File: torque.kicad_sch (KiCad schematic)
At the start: 30 parts, among them U24 ${SIM.PARAMS}, U25 ${SIM.PARAMS}, U26 ${SIM.PARAMS}, U27 ${SIM.PARAMS}, U28 AD5160, U29 AD5160, U30 AD5160, U31 AD5160, U32 AD5160, U33 AD5160, U34 AD5160, U35 AD5160, U92 ${SIM.PARAMS}

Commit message: Before 10K resistors change
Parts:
- R35, R36, R37, R38, R39, R40, R41, R42, R43: footprint (none) -> Resistor_SMD:R_1206_3216Metric_Pad1.30x1.75mm_HandSolder
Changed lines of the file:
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@@
 			)
 		)
-		(property "Footprint" ""
+		(property "Footprint" "Resistor_SMD:R_1206_3216Metric_Pad1.30x1.75mm_HandSolder"
 			(at 215.9 198.628 90)
 			(effects
@@
 			)
 		)
-		(property "Footprint" ""
+		(property "Footprint" "Resistor_SMD:R_1206_3216Metric_Pad1.30x1.75mm_HandSolder"
 			(at 110.49 195.072 90)
 			(effects
@@
 			)
 		)
-		(property "Footprint" ""
+		(property "Footprint" "Resistor_SMD:R_1206_3216Metric_Pad1.30x1.75mm_HandSolder"
 			(at 110.49 151.892 90)
 			(effects
@@
 			)
 		)
-		(property "Footprint" ""
+		(property "Footprint" "Resistor_SMD:R_1206_3216Metric_Pad1.30x1.75mm_HandSolder"
 			(at 95.25 259.842 90)
 			(effects
@@
 			)
 		)
-		(property "Footprint" ""
+		(property "Footprint" "Resistor_SMD:R_1206_3216Metric_Pad1.30x1.75mm_HandSolder"
 			(at 95.25 214.122 90)
 			(effects
@@
 			)
 		)
-		(property "Footprint" ""
+		(property "Footprint" "Resistor_SMD:R_1206_3216Metric_Pad1.30x1.75mm_HandSolder"
 			(at 110.49 108.712 90)
 			(effects
@@
 			)
 		)
-		(property "Footprint" ""
+		(property "Footprint" "Resistor_SMD:R_1206_3216Metric_Pad1.30x1.75mm_HandSolder"
 			(at 110.49 240.792 90)
 			(effects
@@
 			)
 		)
-		(property "Footprint" ""
+		(property "Footprint" "Resistor_SMD:R_1206_3216Metric_Pad1.30x1.75mm_HandSolder"
 			(at 95.25 170.942 90)
 			(effects
@@
 			)
 		)
-		(property "Footprint" ""
+		(property "Footprint" "Resistor_SMD:R_1206_3216Metric_Pad1.30x1.75mm_HandSolder"
 			(at 95.25 127.762 90)
 			(effects

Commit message: Before capcitor update
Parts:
- R35, R36, R37, R38, R39, R40, R41, R42, R43: value R -> 10k
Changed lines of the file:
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@@
 			)
 		)
-		(property "Value" "R"
+		(property "Value" "10k"
 			(at 213.614 200.152 90)
 			(effects
@@
 			)
 		)
-		(property "Value" "R"
+		(property "Value" "10k"
 			(at 110.49 193.04 90)
 			(effects
@@
 			)
 		)
-		(property "Value" "R"
+		(property "Value" "10k"
 			(at 110.49 149.86 90)
 			(effects
@@
 			)
 		)
-		(property "Value" "R"
+		(property "Value" "10k"
 			(at 95.25 257.81 90)
 			(effects
@@
 			)
 		)
-		(property "Value" "R"
+		(property "Value" "10k"
 			(at 95.25 212.09 90)
 			(effects
@@
 			)
 		)
-		(property "Value" "R"
+		(property "Value" "10k"
 			(at 110.49 106.68 90)
 			(effects
@@
 			)
 		)
-		(property "Value" "R"
+		(property "Value" "10k"
 			(at 110.49 238.76 90)
 			(effects
@@
 			)
 		)
-		(property "Value" "R"
+		(property "Value" "10k"
 			(at 95.25 168.91 90)
 			(effects
@@
 			)
 		)
-		(property "Value" "R"
+		(property "Value" "10k"
 			(at 95.25 125.73 90)
 			(effects

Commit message: updated capacitor values
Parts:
- C61, C62, C63, C64, C65, C66, C67, C68: value C -> 100nF
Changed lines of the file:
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@@
 			)
 		)
-		(property "Value" "C"
+		(property "Value" "100nF"
 			(at 190.5 78.7399 0)
 			(effects
@@
 			)
 		)
-		(property "Value" "C"
+		(property "Value" "100nF"
 			(at 162.56 222.2501 0)
 			(effects
@@
 			)
 		)
-		(property "Value" "C"
+		(property "Value" "100nF"
 			(at 162.56 95.2501 0)
 			(effects
@@
 			)
 		)
-		(property "Value" "C"
+		(property "Value" "100nF"
 			(at 190.5 205.7399 0)
 			(effects
@@
 			)
 		)
-		(property "Value" "C"
+		(property "Value" "100nF"
 			(at 190.5 267.9699 0)
 			(effects
@@
 			)
 		)
-		(property "Value" "C"
+		(property "Value" "100nF"
 			(at 190.5 140.9699 0)
 			(effects
@@
 			)
 		)
-		(property "Value" "C"
+		(property "Value" "100nF"
 			(at 162.56 284.4801 0)
 			(effects
@@
 			)
 		)
-		(property "Value" "C"
+		(property "Value" "100nF"
 			(at 162.56 157.4801 0)
 			(effects

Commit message: Updated: power
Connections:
- net -VCC is gone; now on net GND: U24.4 (V-), U25.4 (V-), U26.4 (V-), U27.4 (V-), U92.4 (V-)
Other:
- moved on the sheet: C61, C62, C63, C64, C65, C66, C67, C68

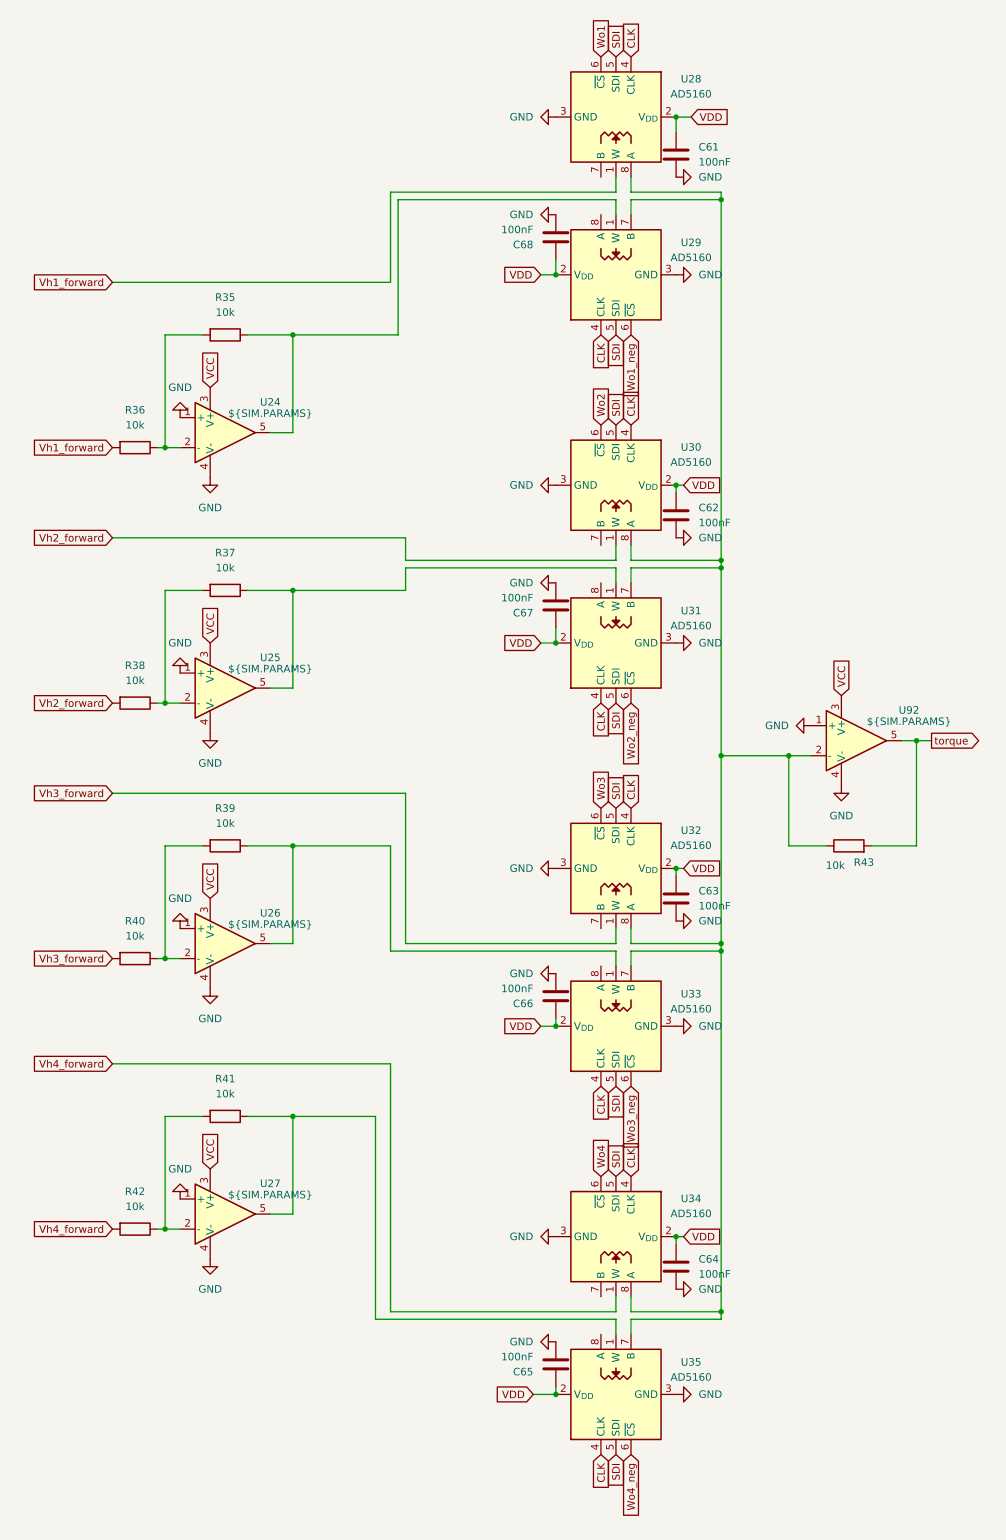
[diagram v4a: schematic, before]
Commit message: Updated: op amps
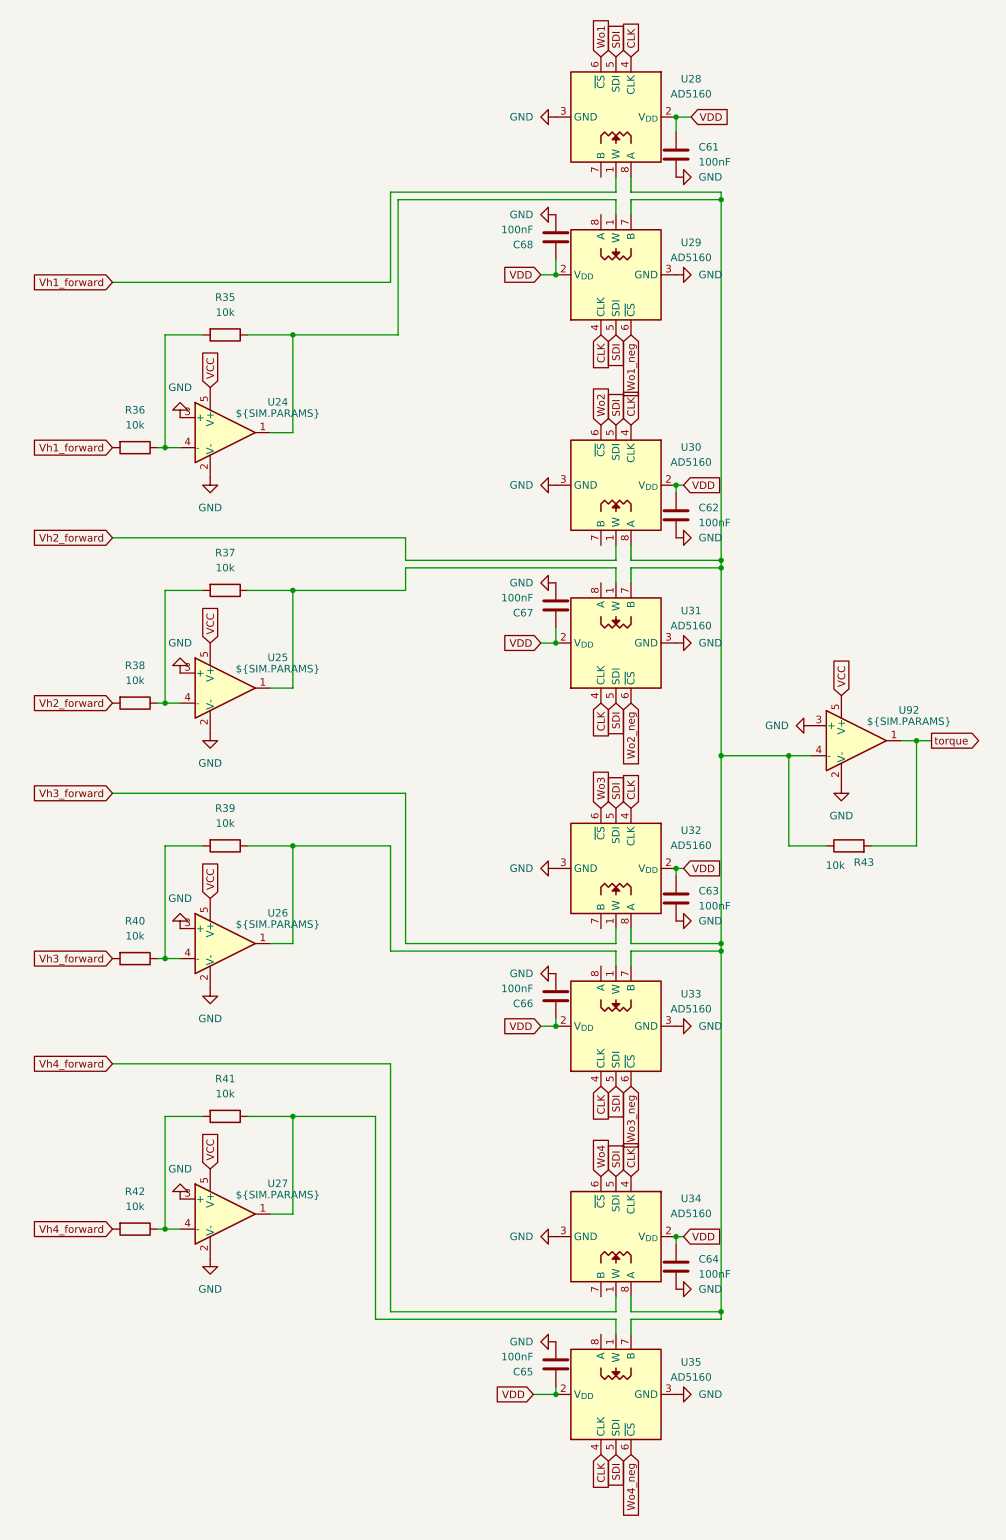
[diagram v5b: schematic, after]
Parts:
- C61, C62, C63, C64, C65, C66, C67, C68: footprint (none) -> Capacitor_SMD:C_1206_3216Metric_Pad1.33x1.80mm_HandSolder
- U24, U25, U26, U27, U92: footprint (none) -> Package_TO_SOT_SMD:SOT-23-5; symbol Simulation_SPICE:OPAMP -> Amplifier_Operational:TLV9061xDBV
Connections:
- net GND: now also U24.2 (V-), U24.3 (+), U25.2 (V-), U25.3 (+), U26.2 (V-), U26.3 (+), U27.2 (V-), U27.3 (+), U92.2 (V-), U92.3 (+); no longer U24.1 (+), U24.4 (V-), U25.1 (+), U25.4 (V-), U26.1 (+), U26.4 (V-), U27.1 (+), U27.4 (V-), U92.1 (+), U92.4 (V-)
- net VCC: now also U24.5 (V+), U25.5 (V+), U26.5 (V+), U27.5 (V+), U92.5 (V+); no longer U24.3 (V+), U25.3 (V+), U26.3 (V+), U27.3 (V+), U92.3 (V+)
- net torque: now also U92.1; no longer U92.5
- net at R43.1, U28.8 (A), U29.7 (B)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: now also U92.4 (-); no longer U92.2 (-)
- net at R37.1, U31.1 (W): now also U25.1; no longer U25.5
- net at R39.1, U33.1 (W): now also U26.1; no longer U26.5
- net at R39.2, R40.1: now also U26.4 (-); no longer U26.2 (-)
- net at R37.2, R38.1: now also U25.4 (-); no longer U25.2 (-)
- net at R41.2, R42.1: now also U27.4 (-); no longer U27.2 (-)
- net at R41.1, U35.1 (W): now also U27.1; no longer U27.5
- net at R35.1, U29.1 (W): now also U24.1; no longer U24.5
- net at R35.2, R36.1: now also U24.4 (-); no longer U24.2 (-)
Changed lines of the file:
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@@
 			)
 		)
-		(property "Footprint" ""
+		(property "Footprint" "Capacitor_SMD:C_1206_3216Metric_Pad1.33x1.80mm_HandSolder"
 			(at 187.6552 83.82 0)
 			(effects
@@
 			)
 		)
-		(property "Footprint" ""
+		(property "Footprint" "Capacitor_SMD:C_1206_3216Metric_Pad1.33x1.80mm_HandSolder"
 			(at 165.4048 218.44 0)
 			(effects
@@
 	)
 	(symbol
-		(lib_id "Simulation_SPICE:OPAMP")
+		(lib_id "Amplifier_Operational:TLV9061xDBV")
 		(at 110.49 170.18 0)
 		(unit 1)
@@
 		(fields_autoplaced yes)
 		(property "Reference" "U25"
-			(at 118.11 165.0298 0)
+			(at 119.38 165.0298 0)
 			(effects
 				(font
@@
 		)
 		(property "Value" "${SIM.PARAMS}"
-			(at 118.11 166.9349 0)
+			(at 119.38 166.9349 0)
 			(effects
 				(font
@@
 			)
 		)
-		(property "Footprint" ""
-			(at 110.49 170.18 0)
+		(property "Footprint" "Package_TO_SOT_SMD:SOT-23-5"
+			(at 95.25 189.23 0)
 			(effects
 				(font
 					(size 1.27 1.27)
 				)
+				(justify left)
 				(hide yes)
 			)
 		)
-		(property "Datasheet" "https://ngspice.sourceforge.io/docs/ngspice-html-manual/manual.xhtml#sec__SUBCKT_Subcircuits"
-			(at 110.49 170.18 0)
+		(property "Datasheet" "https://www.ti.com/lit/ds/symlink/tlv9061.pdf"
+			(at 110.49 149.86 0)
 			(effects
 				(font
@@
 			)
 		)
-		(property "Description" "Operational amplifier, single"
+		(property "Description" "10-MHz, RRIO, CMOS Operational Amplifiers for Cost-Sensitive Systems, SOT-23-5"
 			(at 110.49 170.18 0)
 			(effects
@@
 			)
 		)
-		(property "Footprint" ""
+		(property "Footprint" "Capacitor_SMD:C_1206_3216Metric_Pad1.33x1.80mm_HandSolder"
 			(at 165.4048 90.17 0)
 			(effects
@@
 			)
 		)
-		(property "Footprint" ""
+		(property "Footprint" "Capacitor_SMD:C_1206_3216Metric_Pad1.33x1.80mm_HandSolder"
 			(at 187.6552 209.55 0)
 			(effects
@@
 	)
 	(symbol
-		(lib_id "Simulation_SPICE:OPAMP")
+		(lib_id "Amplifier_Operational:TLV9061xDBV")
 		(at 217.17 179.07 0)
 		(unit 1)
@@
 			)
 		)
-		(property "Footprint" ""
-			(at 217.17 179.07 0)
+		(property "Footprint" "Package_TO_SOT_SMD:SOT-23-5"
+			(at 201.93 198.12 0)
 			(effects
 				(font
 					(size 1.27 1.27)
 				)
+				(justify left)
 				(hide yes)
 			)
 		)
-		(property "Datasheet" "https://ngspice.sourceforge.io/docs/ngspice-html-manual/manual.xhtml#sec__SUBCKT_Subcircuits"
-			(at 217.17 179.07 0)
+		(property "Datasheet" "https://www.ti.com/lit/ds/symlink/tlv9061.pdf"
+			(at 217.17 158.75 0)
 			(effects
 				(font
@@
 			)
 		)
-		(property "Description" "Operational amplifier, single"
+		(property "Description" "10-MHz, RRIO, CMOS Operational Amplifiers for Cost-Sensitive Systems, SOT-23-5"
 			(at 217.17 179.07 0)
 			(effects
@@
 			)
 		)
-		(property "Footprint" ""
+		(property "Footprint" "Capacitor_SMD:C_1206_3216Metric_Pad1.33x1.80mm_HandSolder"
 			(at 187.6552 271.78 0)
 			(effects
@@
 			)
 		)
-		(property "Footprint" ""
+		(property "Footprint" "Capacitor_SMD:C_1206_3216Metric_Pad1.33x1.80mm_HandSolder"
 			(at 187.6552 144.78 0)
 			(effects
@@
 	)
 	(symbol
-		(lib_id "Simulation_SPICE:OPAMP")
+		(lib_id "Amplifier_Operational:TLV9061xDBV")
 		(at 110.49 127 0)
 		(unit 1)
@@
 		(fields_autoplaced yes)
 		(property "Reference" "U24"
-			(at 118.11 121.8498 0)
+			(at 119.38 121.8498 0)
 			(effects
 				(font
@@
 		)
 		(property "Value" "${SIM.PARAMS}"
-			(at 118.11 123.7549 0)
+			(at 119.38 123.7549 0)
 			(effects
 				(font
@@
 			)
 		)
-		(property "Footprint" ""
-			(at 110.49 127 0)
+		(property "Footprint" "Package_TO_SOT_SMD:SOT-23-5"
+			(at 95.25 146.05 0)
 			(effects
 				(font
 					(size 1.27 1.27)
 				)
+				(justify left)
 				(hide yes)
 			)
 		)
-		(property "Datasheet" "https://ngspice.sourceforge.io/docs/ngspice-html-manual/manual.xhtml#sec__SUBCKT_Subcircuits"
-			(at 110.49 127 0)
+		(property "Datasheet" "https://www.ti.com/lit/ds/symlink/tlv9061.pdf"
+			(at 110.49 106.68 0)
 			(effects
 				(font
@@
 			)
 		)
-		(property "Description" "Operational amplifier, single"
+		(property "Description" "10-MHz, RRIO, CMOS Operational Amplifiers for Cost-Sensitive Systems, SOT-23-5"
 			(at 110.49 127 0)
 			(effects
@@
 			)
 		)
-		(property "Footprint" ""
+		(property "Footprint" "Capacitor_SMD:C_1206_3216Metric_Pad1.33x1.80mm_HandSolder"
 			(at 165.4048 280.67 0)
 			(effects
@@
 	)
 	(symbol
-		(lib_id "Simulation_SPICE:OPAMP")
+		(lib_id "Amplifier_Operational:TLV9061xDBV")
 		(at 110.49 213.36 0)
 		(unit 1)
@@
 		(fields_autoplaced yes)
 		(property "Reference" "U26"
-			(at 118.11 208.2098 0)
+			(at 119.38 208.2098 0)
 			(effects
 				(font
@@
 		)
 		(property "Value" "${SIM.PARAMS}"
-			(at 118.11 210.1149 0)
+			(at 119.38 210.1149 0)
 			(effects
 				(font
@@
 			)
 		)
-		(property "Footprint" ""
-			(at 110.49 213.36 0)
+		(property "Footprint" "Package_TO_SOT_SMD:SOT-23-5"
+			(at 95.25 232.41 0)
 			(effects
 				(font
 					(size 1.27 1.27)
 				)
+				(justify left)
 				(hide yes)
 			)
 		)
-		(property "Datasheet" "https://ngspice.sourceforge.io/docs/ngspice-html-manual/manual.xhtml#sec__SUBCKT_Subcircuits"
-			(at 110.49 213.36 0)
+		(property "Datasheet" "https://www.ti.com/lit/ds/symlink/tlv9061.pdf"
+			(at 110.49 193.04 0)
 			(effects
 				(font
@@
 			)
 		)
-		(property "Description" "Operational amplifier, single"
+		(property "Description" "10-MHz, RRIO, CMOS Operational Amplifiers for Cost-Sensitive Systems, SOT-23-5"
 			(at 110.49 213.36 0)
 			(effects
@@
 	)
 	(symbol
-		(lib_id "Simulation_SPICE:OPAMP")
+		(lib_id "Amplifier_Operational:TLV9061xDBV")
 		(at 110.49 259.08 0)
 		(unit 1)
@@
 		(fields_autoplaced yes)
 		(property "Reference" "U27"
-			(at 118.11 253.9298 0)
+			(at 119.38 253.9298 0)
 			(effects
 				(font
@@
 		)
 		(property "Value" "${SIM.PARAMS}"
-			(at 118.11 255.8349 0)
+			(at 119.38 255.8349 0)
 			(effects
 				(font
@@
 			)
 		)
-		(property "Footprint" ""
-			(at 110.49 259.08 0)
+		(property "Footprint" "Package_TO_SOT_SMD:SOT-23-5"
+			(at 95.25 278.13 0)
 			(effects
 				(font
 					(size 1.27 1.27)
 				)
+				(justify left)
 				(hide yes)
 			)
 		)
-		(property "Datasheet" "https://ngspice.sourceforge.io/docs/ngspice-html-manual/manual.xhtml#sec__SUBCKT_Subcircuits"
-			(at 110.49 259.08 0)
+		(property "Datasheet" "https://www.ti.com/lit/ds/symlink/tlv9061.pdf"
+			(at 110.49 238.76 0)
 			(effects
 				(font
@@
 			)
 		)
-		(property "Description" "Operational amplifier, single"
+		(property "Description" "10-MHz, RRIO, CMOS Operational Amplifiers for Cost-Sensitive Systems, SOT-23-5"
 			(at 110.49 259.08 0)
 			(effects
@@
 			)
 		)
-		(property "Footprint" ""
+		(property "Footprint" "Capacitor_SMD:C_1206_3216Metric_Pad1.33x1.80mm_HandSolder"
 			(at 165.4048 152.4 0)
 			(effects

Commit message: Updated: pots
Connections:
- net GND: no longer U24.3 (+), U25.3 (+), U26.3 (+), U27.3 (+), U92.3 (+)
- net VREF: now reaches U32.7 (B)
- net VREF: now also U24.3 (+), U25.3 (+), U26.3 (+), U27.3 (+), U28.7 (B), U29.7 (B), U30.7 (B), U31.7 (B), U33.7 (B), U34.7 (B), U35.7 (B), U92.3 (+)
- net at R43.1, U28.8 (A), U30.8 (A)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: now also U29.8 (A), U31.8 (A), U33.8 (A), U35.8 (A); no longer U29.7 (B), U31.7 (B), U33.7 (B), U35.7 (B)
